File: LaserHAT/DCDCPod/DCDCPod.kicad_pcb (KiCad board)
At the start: 2 copper layers, 31 x 19.5 mm, 17 parts, among them J1 5V IN (HAT J103), J2 +/-V OUT (HAT J102), Q101 MMBT3904, Q102 MMBT3906

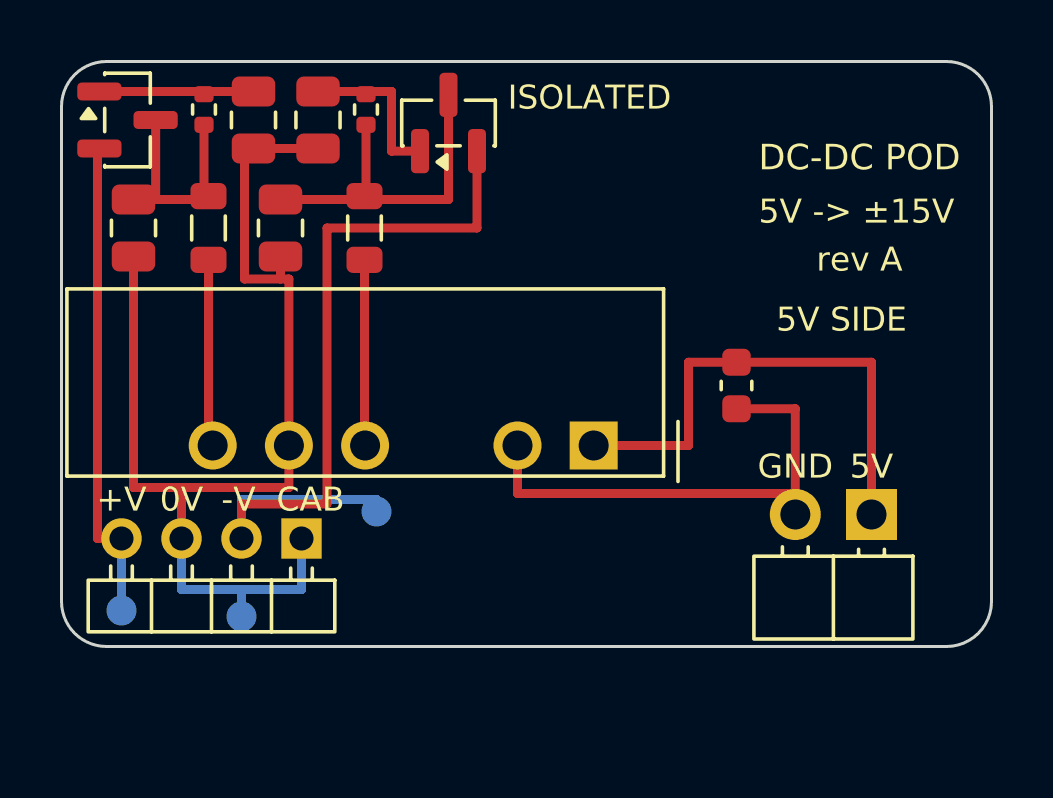
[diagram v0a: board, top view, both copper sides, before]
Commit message: DCDCPod: turned around - parts face south, PS1 on the top edge above the BNC bodies
Resolves the pod-vs-bonnet depth conflict without moving the HAT's J102/J103 rows (y 39.0): the
pod's bare back now faces the bonnet with 5.1-5.4 mm to spare, PS1's body sits 16.6-22.6 mm above
the HAT (1.0 mm over the BNC tops) hanging south over J6/J7, the low parts face the BNCs with 5 mm
of room.  Pod 31 x 22.5 mm, 1.6 mm thick; header footprints mirrored along their rows so the pins
still land on the same HAT holes (HAT x = pod x + 15); placement, routing, rule areas, isolation
check, fab outputs and renders regenerated (DRC 0/0/0, isolation gap 3.48 mm).  StimHAT: pod
outline and PS1 overhang redrawn on User.Drawings, README pod section updated.

Co-Authored-By: Claude Fable 5.1 <noreply@anthropic.com>
Claude-Session: https://claude.ai/code/session_015kiXLxnPpBaXdXJu2EMvn7
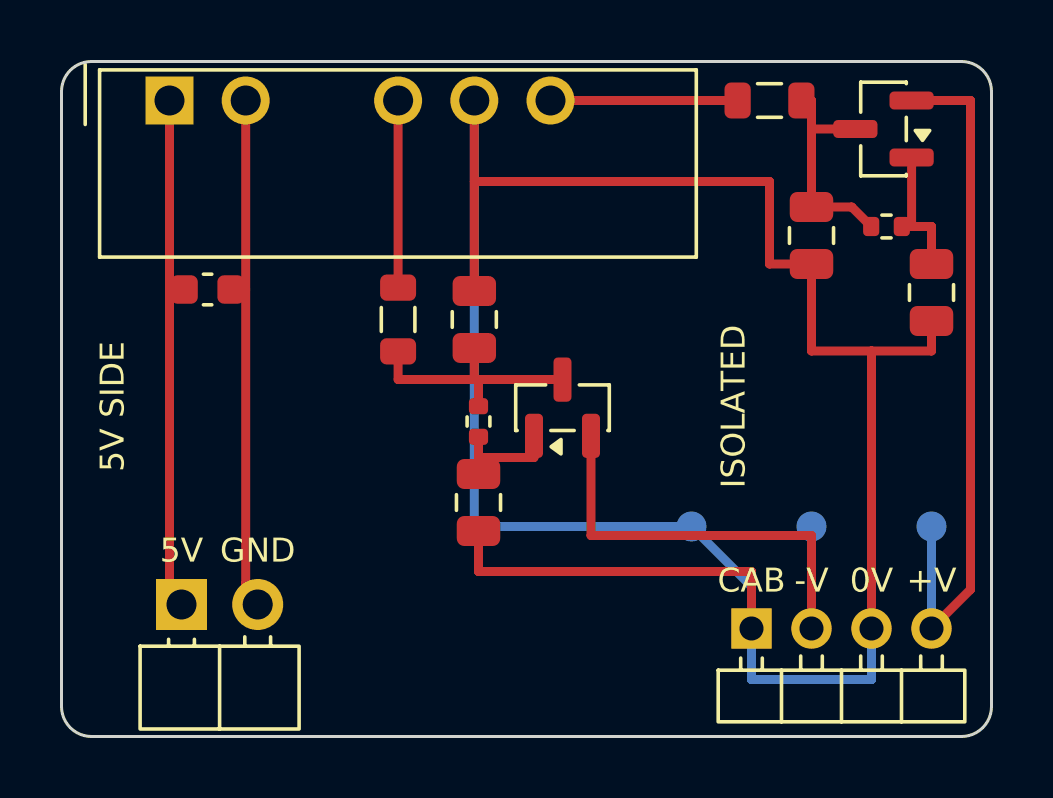
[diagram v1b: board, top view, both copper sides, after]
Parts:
- moved TP1 27.1 mm to (29.0, 15.5)
- moved Q101 25.2 mm to (27.4, 2.25), turned to 180 degrees
- moved C107 23.3 mm to (29.0, 7.70)
- moved R111 23.1 mm to (27.5, 5.50), turned to 0 degrees
- moved C105 22.6 mm to (25.0, 5.80)
- moved J2 21.2 mm to (29.0, 18.9)
- moved J1 20.7 mm to (6.54, 18.1)
- moved L101 19.2 mm to (23.6, 1.30), turned to 0 degrees
- moved PS1 18.2 mm to (3.60, 1.30), turned to 0 degrees
- moved C104 17.9 mm to (4.87, 7.60), turned to 0 degrees
- moved TP2 15.3 mm to (21.0, 15.5)
- moved TP3 14.5 mm to (25.0, 15.5)
- moved C108 13.8 mm to (13.9, 14.7)
- moved R112 11.1 mm to (13.9, 12.0), turned to 90 degrees
- moved Q102 10.2 mm to (16.7, 11.5)
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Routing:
- net 0V: track 38.7 -> 82.9 mm
- net -V_OUT: track 27.0 -> 17.2 mm
- net +V_OUT: track 16.3 -> 23.5 mm
- net /-V_F: track 11.6 -> 8.36 mm
- net /QB_N: track 5.39 -> 3.81 mm
- net GND: track 16.3 -> 17.4 mm
- net /QB_P: track 5.14 -> 4.54 mm
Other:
- board size 31 x 19.5 mm -> 31 x 22.5 mm
- board text added: "5V -> ±15V rev A"
- board text removed: "5V -> ±15V"
- board text removed: "DC-DC POD rev A"
- board text removed: "rev A"

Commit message: DCDCPod: converter footprint for the fitted RECOM RB-0515D/HP
New dcdcpod:DCDC_SIP6_RB0515D generated from the RECOM RB drawing (pins 1.27 mm behind / 4.73 mm
in front of the marked face, pin 1 2.0 mm from the end, 19.6 x 6.0 x 10.2 body on 0.5 mm standoffs
in the model; same 1-2-4-5-6 holes) replaces the copy of the Mornsun footprint; PS1's value is
RB-0515D/HP and it moved 0.4 mm down the pod so the body stays 0.43 mm inside the top edge (z
16.57-22.57, 0.97 mm over the BNC tops).  Body side confirmed from both datasheets; the README's
open point is closed.  DRC 0/0/0, isolation OK, fab outputs and renders regenerated.

Co-Authored-By: Claude Fable 5.1 <noreply@anthropic.com>
Claude-Session: https://claude.ai/code/session_015kiXLxnPpBaXdXJu2EMvn7
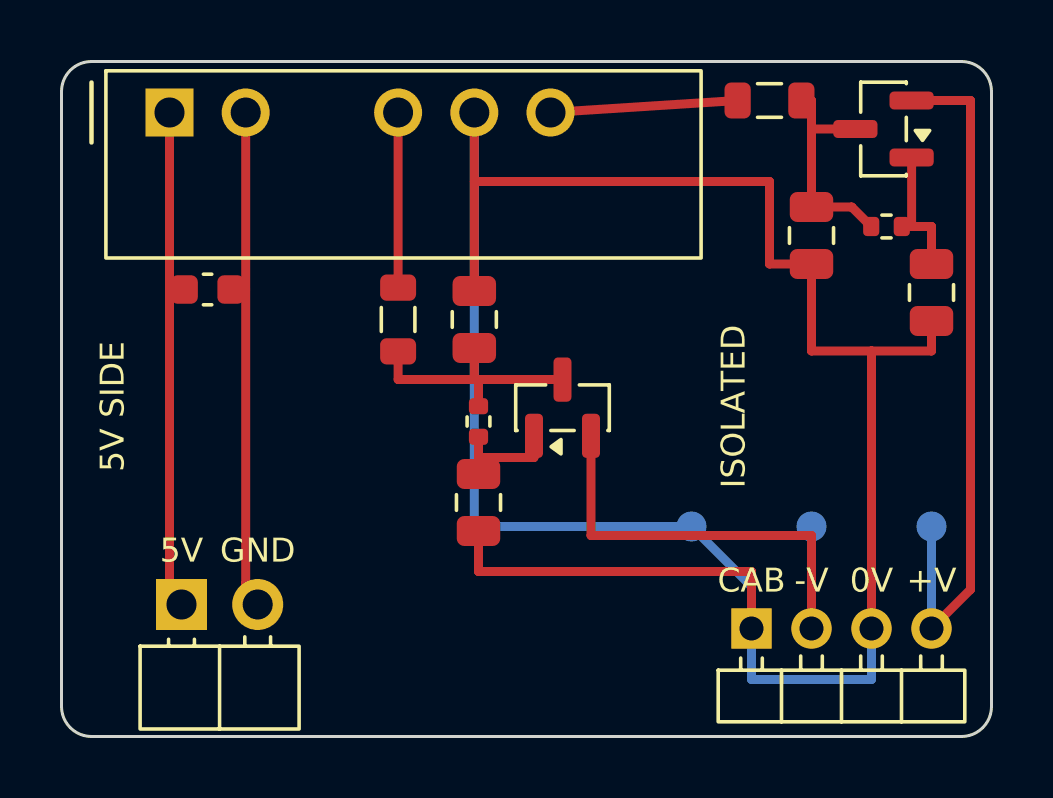
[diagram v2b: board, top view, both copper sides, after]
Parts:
- PS1: value A0515S-1WR3 -> RB-0515D/HP; footprint dcdcpod:DCDC_SIP6_A0515S_BodyN -> dcdcpod:DCDC_SIP6_RB0515D
- moved PS1 0.40 mm to (3.60, 1.70)
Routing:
- net 0V: track 82.9 -> 82.1 mm
